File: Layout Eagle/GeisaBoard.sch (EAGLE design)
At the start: 19 parts, among them X1 22-23-2021

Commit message: GeisaBoard layout completo (espero)
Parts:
- removed Q2: (no value), transistor-power:PMOSFET_PTO220BV
- removed R3: (no value), rcl:R-US_0204/7
- added Q1: IRF540, transistor-power:IRF540
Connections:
- removed net N$1: DB9.1, Q2.D
- net GND: now also Q1.S; no longer DB9.5
- net LEIRASATIVAS: now also Q1.G; no longer Q2.G
- net N$2: now also DB9.5, Q1.D; no longer Q2.S, R3.1
- net VCC: now also DB9.1; no longer R3.2
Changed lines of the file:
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@@
 <part name="X1" library="con-molex" library_urn="urn:adsk.eagle:library:165" deviceset="22-23-2021" device=""/>
 <part name="FRAME1" library="frames" library_urn="urn:adsk.eagle:library:229" deviceset="DINA4_L" device=""/>
-<part name="R3" library="rcl" library_urn="urn:adsk.eagle:library:334" deviceset="R-US_" device="0204/7" package3d_urn="urn:adsk.eagle:package:23498/1"/>
-<part name="Q2" library="transistor-power" library_urn="urn:adsk.eagle:library:400" deviceset="PMOSFET_P" device="TO220BV" package3d_urn="urn:adsk.eagle:package:29484/3"/>
+<part name="Q1" library="transistor-power" library_urn="urn:adsk.eagle:library:400" deviceset="IRF540" device="" package3d_urn="urn:adsk.eagle:package:29484/3"/>
 </parts>
 <sheets>
@@
 <instance part="R9" gate="G$1" x="-109.22" y="53.34" rot="R90"/>
 <instance part="RESET" gate="G$1" x="-109.22" y="40.64"/>
-<instance part="GND6" gate="1" x="25.4" y="10.16" rot="MR0"/>
-<instance part="SUPPLY9" gate="G$1" x="20.32" y="63.5"/>
+<instance part="GND6" gate="1" x="25.4" y="-7.62" rot="MR0"/>
+<instance part="SUPPLY9" gate="G$1" x="20.32" y="38.1"/>
 <instance part="GND12" gate="1" x="76.2" y="91.44"/>
 <instance part="GND13" gate="1" x="-96.52" y="-12.7"/>
@@
 <instance part="FRAME1" gate="G$1" x="-137.16" y="-50.8"/>
 <instance part="FRAME1" gate="G$2" x="25.4" y="-50.8"/>
-<instance part="R3" gate="G$1" x="20.32" y="53.34" rot="R90"/>
-<instance part="Q2" gate="G$1" x="17.78" y="40.64"/>
+<instance part="Q1" gate="G$1" x="22.86" y="5.08"/>
 </instances>
 <busses>
@@
 </segment>
 <segment>
-<wire x1="12.7" y1="43.18" x2="2.54" y2="43.18" width="0.1524" layer="91"/>
-<label x="0" y="43.18" size="1.778" layer="95"/>
-<pinref part="Q2" gate="G$1" pin="G"/>
+<pinref part="Q1" gate="G$1" pin="G"/>
+<wire x1="20.32" y1="2.54" x2="2.54" y2="2.54" width="0.1524" layer="91"/>
+<label x="2.54" y="2.54" size="1.778" layer="95"/>
 </segment>
 </net>
@@
 </segment>
 <segment>
-<pinref part="GND6" gate="1" pin="GND"/>
-<wire x1="25.4" y1="15.24" x2="25.4" y2="12.7" width="0.1524" layer="91"/>
-<pinref part="DB9" gate="G$1" pin="5"/>
-<wire x1="27.94" y1="15.24" x2="25.4" y2="15.24" width="0.1524" layer="91"/>
-</segment>
-<segment>
 <pinref part="GND17" gate="1" pin="GND"/>
 <wire x1="86.36" y1="30.48" x2="93.98" y2="30.48" width="0.1524" layer="91"/>
@@
 <wire x1="-83.82" y1="86.36" x2="-91.44" y2="86.36" width="0.1524" layer="91"/>
 <wire x1="-91.44" y1="86.36" x2="-91.44" y2="78.74" width="0.1524" layer="91"/>
+</segment>
+<segment>
+<pinref part="Q1" gate="G$1" pin="S"/>
+<pinref part="GND6" gate="1" pin="GND"/>
+<wire x1="25.4" y1="0" x2="25.4" y2="-5.08" width="0.1524" layer="91"/>
 </segment>
 </net>
@@
 </segment>
 <segment>
-<pinref part="R3" gate="G$1" pin="2"/>
+<wire x1="27.94" y1="25.4" x2="20.32" y2="25.4" width="0.1524" layer="91"/>
+<pinref part="DB9" gate="G$1" pin="1"/>
+<wire x1="20.32" y1="25.4" x2="20.32" y2="38.1" width="0.1524" layer="91"/>
 <pinref part="SUPPLY9" gate="G$1" pin="VCC"/>
-<wire x1="20.32" y1="58.42" x2="20.32" y2="63.5" width="0.1524" layer="91"/>
 </segment>
 </net>
@@
 </segment>
 </net>
-<net name="N$1" class="1">
-<segment>
-<wire x1="27.94" y1="25.4" x2="20.32" y2="25.4" width="0.1524" layer="91"/>
-<pinref part="DB9" gate="G$1" pin="1"/>
-<wire x1="20.32" y1="25.4" x2="20.32" y2="35.56" width="0.1524" layer="91"/>
-<pinref part="Q2" gate="G$1" pin="D"/>
-</segment>
-</net>
-<net name="N$2" class="0">
-<segment>
-<pinref part="R3" gate="G$1" pin="1"/>
-<wire x1="20.32" y1="45.72" x2="20.32" y2="48.26" width="0.1524" layer="91"/>
-<pinref part="Q2" gate="G$1" pin="S"/>
-</segment>
-</net>
+<net name="N$2" class="1">
+<segment>
+<pinref part="DB9" gate="G$1" pin="5"/>
+<wire x1="27.94" y1="15.24" x2="25.4" y2="15.24" width="0.1524" layer="91"/>
+<pinref part="Q1" gate="G$1" pin="D"/>
+<wire x1="25.4" y1="10.16" x2="25.4" y2="15.24" width="0.1524" layer="91"/>
+</segment>
+</net>

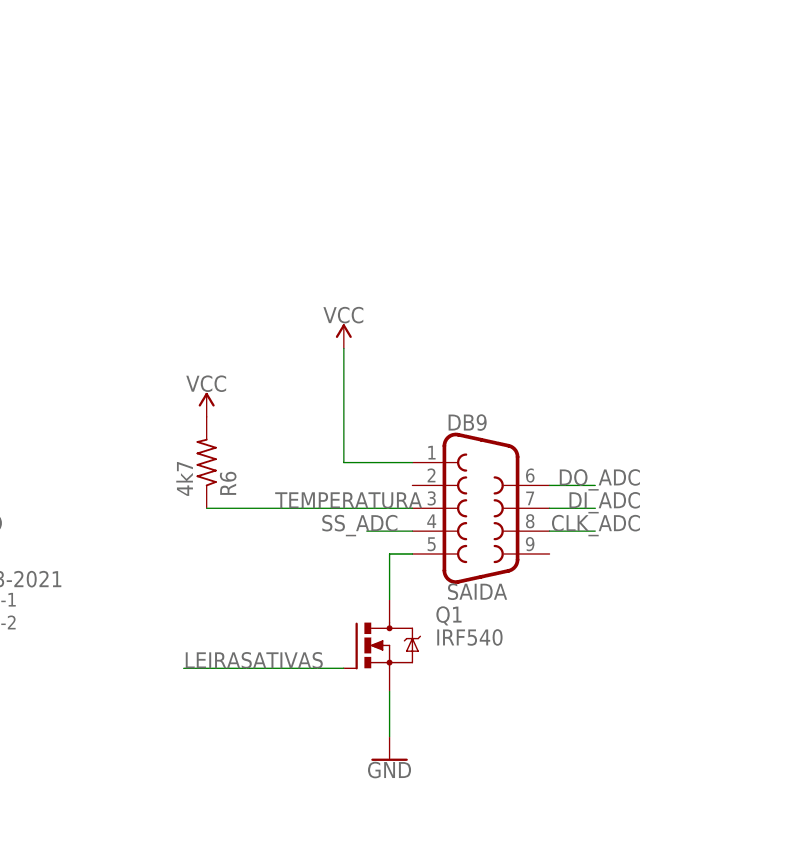
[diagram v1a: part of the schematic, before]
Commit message: Resistor de pull-down colocado no chaveamento do transistor de potência
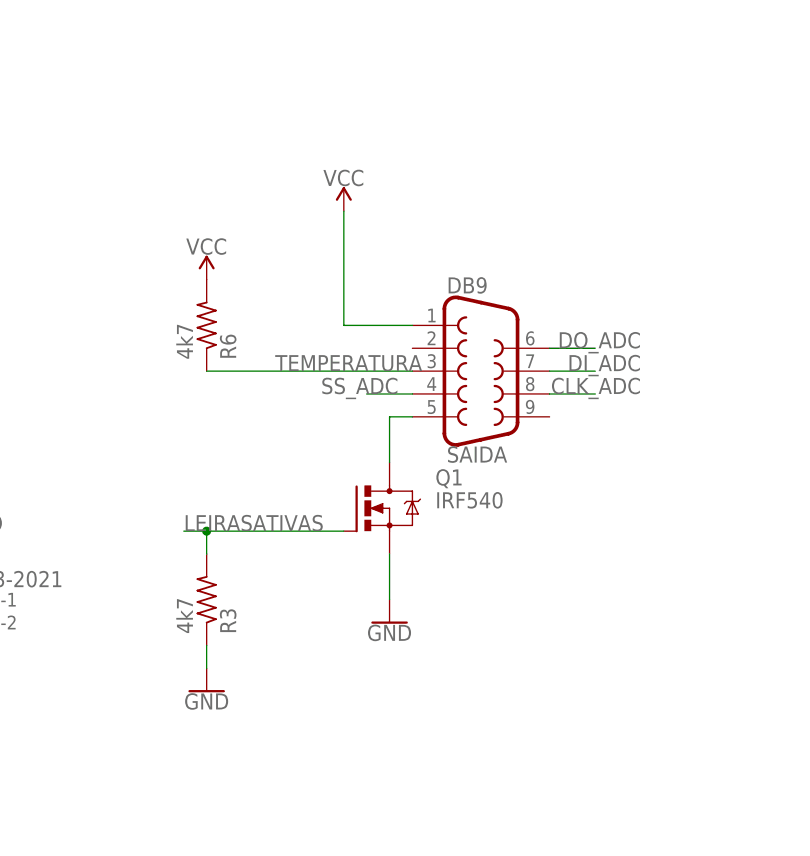
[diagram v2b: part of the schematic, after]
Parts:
- added R3: 4k7, rcl:R-US_0204/7
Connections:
- net GND: now also R3.1
- net LEIRASATIVAS: now also R3.2
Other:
- moved on the sheet: DB9, Q1, R6
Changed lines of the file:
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@@
 <part name="FRAME1" library="frames" library_urn="urn:adsk.eagle:library:229" deviceset="DINA4_L" device=""/>
 <part name="Q1" library="transistor-power" library_urn="urn:adsk.eagle:library:400" deviceset="IRF540" device="" package3d_urn="urn:adsk.eagle:package:29484/3"/>
+<part name="R3" library="rcl" library_urn="urn:adsk.eagle:library:334" deviceset="R-US_" device="0204/7" package3d_urn="urn:adsk.eagle:package:23498/1" value="4k7"/>
+<part name="GND1" library="SparkFun-PowerSymbols" deviceset="GND" device=""/>
 </parts>
 <sheets>
@@
 <instance part="R9" gate="G$1" x="-109.22" y="53.34" rot="R90"/>
 <instance part="RESET" gate="G$1" x="-109.22" y="40.64"/>
-<instance part="GND6" gate="1" x="25.4" y="-7.62" rot="MR0"/>
-<instance part="SUPPLY9" gate="G$1" x="20.32" y="38.1"/>
+<instance part="GND6" gate="1" x="25.4" y="7.62" rot="MR0"/>
+<instance part="SUPPLY9" gate="G$1" x="20.32" y="53.34"/>
 <instance part="GND12" gate="1" x="76.2" y="91.44"/>
 <instance part="GND13" gate="1" x="-96.52" y="-12.7"/>
@@
 <instance part="SUPPLY1" gate="G$1" x="-10.16" y="111.76"/>
 <instance part="SUPPLY2" gate="G$1" x="-15.24" y="106.68" rot="MR0"/>
-<instance part="DB9" gate="G$1" x="35.56" y="20.32"/>
+<instance part="DB9" gate="G$1" x="35.56" y="35.56"/>
 <instance part="RTC" gate="G$1" x="22.86" y="99.06"/>
 <instance part="SD" gate="G$1" x="104.14" y="99.06"/>
 <instance part="GND5" gate="1" x="-91.44" y="76.2"/>
-<instance part="R6" gate="G$1" x="5.08" y="25.4" rot="MR90"/>
-<instance part="SUPPLY11" gate="G$1" x="5.08" y="30.48" rot="MR0"/>
+<instance part="R6" gate="G$1" x="5.08" y="40.64" rot="MR90"/>
+<instance part="SUPPLY11" gate="G$1" x="5.08" y="45.72" rot="MR0"/>
 <instance part="VCC_LIGAR_BLUETOOTH" gate="1" x="-101.6" y="114.3"/>
 <instance part="SINAL_LIGAR_BLUETOOTH" gate="1" x="-96.52" y="106.68"/>
@@
 <instance part="FRAME1" gate="G$1" x="-137.16" y="-50.8"/>
 <instance part="FRAME1" gate="G$2" x="25.4" y="-50.8"/>
-<instance part="Q1" gate="G$1" x="22.86" y="5.08"/>
+<instance part="Q1" gate="G$1" x="22.86" y="20.32"/>
+<instance part="R3" gate="G$1" x="5.08" y="10.16" rot="MR90"/>
+<instance part="GND1" gate="1" x="5.08" y="0" rot="MR0"/>
 </instances>
 <busses>
@@
 <segment>
 <pinref part="Q1" gate="G$1" pin="G"/>
-<wire x1="20.32" y1="2.54" x2="2.54" y2="2.54" width="0.1524" layer="91"/>
-<label x="2.54" y="2.54" size="1.778" layer="95"/>
+<wire x1="20.32" y1="17.78" x2="5.08" y2="17.78" width="0.1524" layer="91"/>
+<label x="2.54" y="17.78" size="1.778" layer="95"/>
+<pinref part="R3" gate="G$1" pin="2"/>
+<wire x1="5.08" y1="17.78" x2="2.54" y2="17.78" width="0.1524" layer="91"/>
+<wire x1="5.08" y1="15.24" x2="5.08" y2="17.78" width="0.1524" layer="91"/>
+<junction x="5.08" y="17.78"/>
 </segment>
 </net>
@@
 <pinref part="Q1" gate="G$1" pin="S"/>
 <pinref part="GND6" gate="1" pin="GND"/>
-<wire x1="25.4" y1="0" x2="25.4" y2="-5.08" width="0.1524" layer="91"/>
+<wire x1="25.4" y1="15.24" x2="25.4" y2="10.16" width="0.1524" layer="91"/>
+</segment>
+<segment>
+<pinref part="GND1" gate="1" pin="GND"/>
+<pinref part="R3" gate="G$1" pin="1"/>
+<wire x1="5.08" y1="2.54" x2="5.08" y2="5.08" width="0.1524" layer="91"/>
 </segment>
 </net>
@@
 </segment>
 <segment>
-<label x="12.7" y="20.32" size="1.778" layer="95"/>
+<label x="12.7" y="35.56" size="1.778" layer="95"/>
 <pinref part="DB9" gate="G$1" pin="3"/>
 <pinref part="R6" gate="G$1" pin="1"/>
-<wire x1="5.08" y1="20.32" x2="27.94" y2="20.32" width="0.1524" layer="91"/>
+<wire x1="5.08" y1="35.56" x2="27.94" y2="35.56" width="0.1524" layer="91"/>
 </segment>
 </net>
@@
 </segment>
 <segment>
-<wire x1="27.94" y1="25.4" x2="20.32" y2="25.4" width="0.1524" layer="91"/>
+<wire x1="27.94" y1="40.64" x2="20.32" y2="40.64" width="0.1524" layer="91"/>
 <pinref part="DB9" gate="G$1" pin="1"/>
-<wire x1="20.32" y1="25.4" x2="20.32" y2="38.1" width="0.1524" layer="91"/>
+<wire x1="20.32" y1="40.64" x2="20.32" y2="53.34" width="0.1524" layer="91"/>
 <pinref part="SUPPLY9" gate="G$1" pin="VCC"/>
 </segment>
@@
 </segment>
 <segment>
-<wire x1="27.94" y1="17.78" x2="22.86" y2="17.78" width="0.1524" layer="91"/>
-<label x="17.78" y="17.78" size="1.778" layer="95"/>
+<wire x1="27.94" y1="33.02" x2="22.86" y2="33.02" width="0.1524" layer="91"/>
+<label x="17.78" y="33.02" size="1.778" layer="95"/>
 <pinref part="DB9" gate="G$1" pin="4"/>
 </segment>
@@
 </segment>
 <segment>
-<wire x1="43.18" y1="17.78" x2="48.26" y2="17.78" width="0.1524" layer="91"/>
-<label x="53.34" y="17.78" size="1.778" layer="95" rot="MR0"/>
+<wire x1="43.18" y1="33.02" x2="48.26" y2="33.02" width="0.1524" layer="91"/>
+<label x="53.34" y="33.02" size="1.778" layer="95" rot="MR0"/>
 <pinref part="DB9" gate="G$1" pin="8"/>
 </segment>
@@
 </segment>
 <segment>
-<wire x1="43.18" y1="22.86" x2="48.26" y2="22.86" width="0.1524" layer="91"/>
-<label x="53.34" y="22.86" size="1.778" layer="95" rot="MR0"/>
+<wire x1="43.18" y1="38.1" x2="48.26" y2="38.1" width="0.1524" layer="91"/>
+<label x="53.34" y="38.1" size="1.778" layer="95" rot="MR0"/>
 <pinref part="DB9" gate="G$1" pin="6"/>
 </segment>
@@
 </segment>
 <segment>
-<wire x1="43.18" y1="20.32" x2="48.26" y2="20.32" width="0.1524" layer="91"/>
-<label x="53.34" y="20.32" size="1.778" layer="95" rot="MR0"/>
+<wire x1="43.18" y1="35.56" x2="48.26" y2="35.56" width="0.1524" layer="91"/>
+<label x="53.34" y="35.56" size="1.778" layer="95" rot="MR0"/>
 <pinref part="DB9" gate="G$1" pin="7"/>
 </segment>
@@
 <segment>
 <pinref part="DB9" gate="G$1" pin="5"/>
-<wire x1="27.94" y1="15.24" x2="25.4" y2="15.24" width="0.1524" layer="91"/>
+<wire x1="27.94" y1="30.48" x2="25.4" y2="30.48" width="0.1524" layer="91"/>
 <pinref part="Q1" gate="G$1" pin="D"/>
-<wire x1="25.4" y1="10.16" x2="25.4" y2="15.24" width="0.1524" layer="91"/>
-</segment>
-</net>
+<wire x1="25.4" y1="25.4" x2="25.4" y2="30.48" width="0.1524" layer="91"/>
+</segment>
+</net>

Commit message: Versão Final da GeisaBoard
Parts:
- added MICRO_USB: (no value), SparkFun-Connectors:USB_MICRO-BREDUCED_PASTE
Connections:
- net GND: now also MICRO_USB.GND
- net VCC: now also MICRO_USB.VBUS
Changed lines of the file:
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@@
 <part name="R3" library="rcl" library_urn="urn:adsk.eagle:library:334" deviceset="R-US_" device="0204/7" package3d_urn="urn:adsk.eagle:package:23498/1" value="4k7"/>
 <part name="GND1" library="SparkFun-PowerSymbols" deviceset="GND" device=""/>
+<part name="MICRO_USB" library="SparkFun-Connectors" library_urn="urn:adsk.eagle:library:513" deviceset="USB_MICRO-B" device="REDUCED_PASTE" package3d_urn="urn:adsk.eagle:package:38239/1"/>
+<part name="SUPPLY3" library="SparkFun-PowerSymbols" deviceset="VCC" device=""/>
+<part name="GND2" library="SparkFun-PowerSymbols" deviceset="GND" device=""/>
 </parts>
 <sheets>
@@
 <instance part="R3" gate="G$1" x="5.08" y="10.16" rot="MR90"/>
 <instance part="GND1" gate="1" x="5.08" y="0" rot="MR0"/>
+<instance part="MICRO_USB" gate="G$1" x="88.9" y="60.96"/>
+<instance part="SUPPLY3" gate="G$1" x="76.2" y="71.12"/>
+<instance part="GND2" gate="1" x="76.2" y="50.8"/>
 </instances>
 <busses>
@@
 <pinref part="R3" gate="G$1" pin="1"/>
 <wire x1="5.08" y1="2.54" x2="5.08" y2="5.08" width="0.1524" layer="91"/>
+</segment>
+<segment>
+<pinref part="MICRO_USB" gate="G$1" pin="GND"/>
+<pinref part="GND2" gate="1" pin="GND"/>
+<wire x1="83.82" y1="55.88" x2="76.2" y2="55.88" width="0.1524" layer="91"/>
+<wire x1="76.2" y1="55.88" x2="76.2" y2="53.34" width="0.1524" layer="91"/>
 </segment>
 </net>
@@
 <pinref part="SUPPLY9" gate="G$1" pin="VCC"/>
 </segment>
-</net>
+<segment>
+<pinref part="MICRO_USB" gate="G$1" pin="VBUS"/>
+<pinref part="SUPPLY3" gate="G$1" pin="VCC"/>
+<wire x1="83.82" y1="66.04" x2="76.2" y2="66.04" width="0.1524" layer="91"/>
+<wire x1="76.2" y1="66.04" x2="76.2" y2="71.12" width="0.1524" layer="91"/>
+</segment>
+</net>

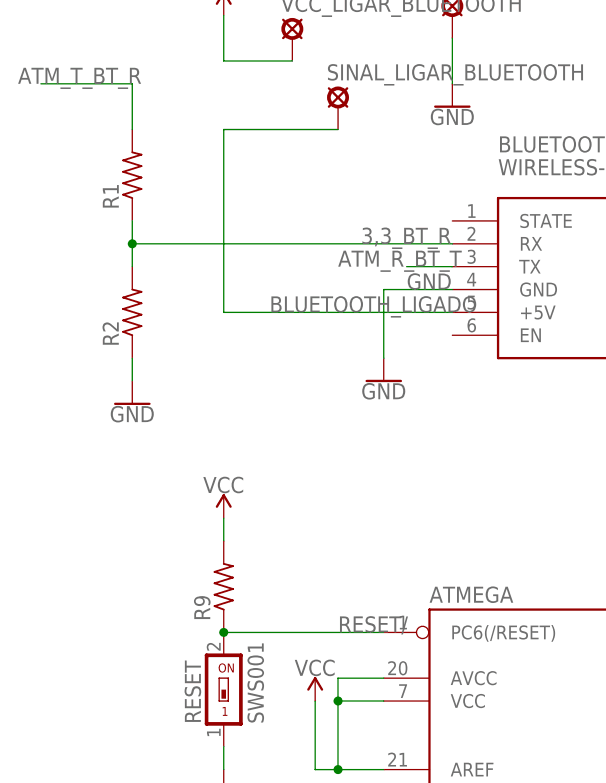
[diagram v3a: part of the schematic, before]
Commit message: Valores de resistores colocados
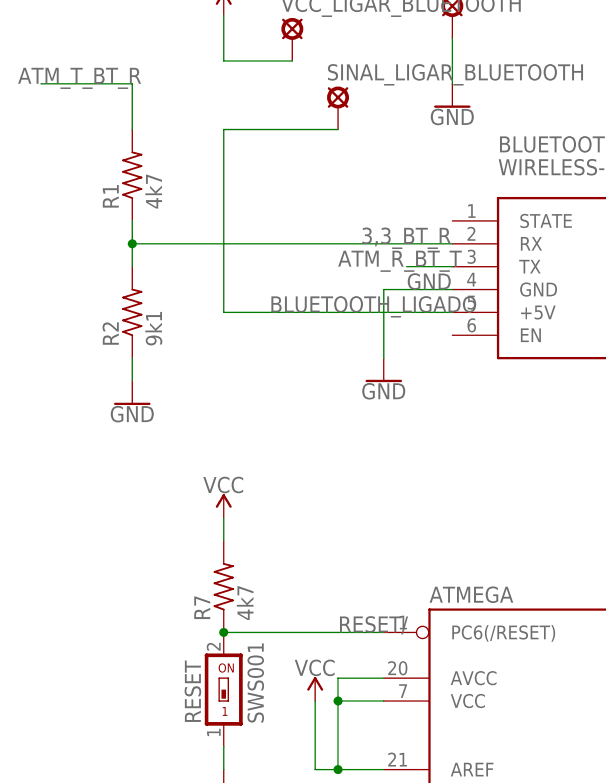
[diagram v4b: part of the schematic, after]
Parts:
- R1, R7: value (none) -> 4k7
- R2: value (none) -> 9k1
- renumbered R9 to R7
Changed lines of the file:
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@@
 <part name="ATMEGA" library="SparkFun-IC-Microcontroller" deviceset="ATMEGA328P_PDIP" device="" value="328P"/>
 <part name="BLUETOOTH" library="diy-modules" deviceset="WIRELESS-BLUETOOTH-HC-05" device=""/>
-<part name="R1" library="rcl" library_urn="urn:adsk.eagle:library:334" deviceset="R-US_" device="0204/7" package3d_urn="urn:adsk.eagle:package:23498/1"/>
-<part name="R2" library="rcl" library_urn="urn:adsk.eagle:library:334" deviceset="R-US_" device="0204/7" package3d_urn="urn:adsk.eagle:package:23498/1"/>
-<part name="R9" library="rcl" library_urn="urn:adsk.eagle:library:334" deviceset="R-US_" device="0204/7" package3d_urn="urn:adsk.eagle:package:23498/1"/>
+<part name="R1" library="rcl" library_urn="urn:adsk.eagle:library:334" deviceset="R-US_" device="0204/7" package3d_urn="urn:adsk.eagle:package:23498/1" value="4k7"/>
+<part name="R2" library="rcl" library_urn="urn:adsk.eagle:library:334" deviceset="R-US_" device="0204/7" package3d_urn="urn:adsk.eagle:package:23498/1" value="9k1"/>
+<part name="R7" library="rcl" library_urn="urn:adsk.eagle:library:334" deviceset="R-US_" device="0204/7" package3d_urn="urn:adsk.eagle:package:23498/1" value="4k7"/>
 <part name="RESET" library="smd-special" library_urn="urn:adsk.eagle:library:362" deviceset="SWS001" device="" package3d_urn="urn:adsk.eagle:package:26467/1"/>
 <part name="GND6" library="SparkFun-PowerSymbols" deviceset="GND" device=""/>
@@
 <instance part="R1" gate="G$1" x="-119.38" y="99.06" rot="R90"/>
 <instance part="R2" gate="G$1" x="-119.38" y="83.82" rot="R90"/>
-<instance part="R9" gate="G$1" x="-109.22" y="53.34" rot="R90"/>
+<instance part="R7" gate="G$1" x="-109.22" y="53.34" rot="R90"/>
 <instance part="RESET" gate="G$1" x="-109.22" y="40.64"/>
 <instance part="GND6" gate="1" x="25.4" y="7.62" rot="MR0"/>
@@
 <segment>
 <pinref part="RESET" gate="G$1" pin="2"/>
-<pinref part="R9" gate="G$1" pin="1"/>
+<pinref part="R7" gate="G$1" pin="1"/>
 <pinref part="ATMEGA" gate="G$1" pin="PC6(/RESET)"/>
 <wire x1="-91.44" y1="48.26" x2="-109.22" y2="48.26" width="0.1524" layer="91"/>
@@
 </segment>
 <segment>
-<pinref part="R9" gate="G$1" pin="2"/>
+<pinref part="R7" gate="G$1" pin="2"/>
 <pinref part="SUPPLY13" gate="G$1" pin="VCC"/>
 <wire x1="-109.22" y1="60.96" x2="-109.22" y2="58.42" width="0.1524" layer="91"/>
